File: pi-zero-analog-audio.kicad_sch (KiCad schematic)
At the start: 6 parts, among them J1 GPIO, U1 CAT24C256

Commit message: Unrouted
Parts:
- removed C1: 100n, symbol Device:C_Small
- removed JP1: ID_WP, symbol Jumper:SolderJumper_2_Open
- removed R1, R2: 3.9k, symbol Device:R_Small
- removed U1: CAT24C256, symbol Memory_EEPROM:CAT24C256
- added C1: 1u, Capacitor_SMD:C_0805_2012Metric_Pad1.18x1.45mm_HandSolder, symbol Device:C
- added C2: 4.7u, Capacitor_SMD:C_0805_2012Metric_Pad1.18x1.45mm_HandSolder, symbol Device:C
- added C3, C6: 47u, Capacitor_SMD:C_0805_2012Metric_Pad1.18x1.45mm_HandSolder, symbol Device:C_Polarized
- added C4, C5, C7: 100n, Capacitor_SMD:C_0805_2012Metric_Pad1.18x1.45mm_HandSolder, symbol Device:C
- added J2: SJ1-3555NG-BE, CUI_SJ1-3555NG-BE, symbol SJ1-3555NG-BE:SJ1-3555NG-BE
- added R1, R4: 220R, Resistor_SMD:R_0805_2012Metric_Pad1.20x1.40mm_HandSolder, symbol Device:R
- added R2, R5: 100R, Resistor_SMD:R_0805_2012Metric_Pad1.20x1.40mm_HandSolder, symbol Device:R
- added R3, R6: 1.8k, Resistor_SMD:R_0805_2012Metric_Pad1.20x1.40mm_HandSolder, symbol Device:R
- added U1: LP5907MFX-3.3, Package_TO_SOT_SMD:SOT-23-5, symbol Regulator_Linear:LP5907MFX-3.3
- added U2: 74LVC2G34, Package_TO_SOT_SMD:SOT-23-6_Handsoldering, symbol 74xGxx:74LVC2G34
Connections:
- net +5V: now also C1.1, U1.1 (IN), U1.3 (EN)
- net GND: now also C1.2, C2.2, C4.2, C5.2, C7.2, J2.1, R2.2, R3.2, R5.2, R6.2, U1.2 (GND), U2.2 (GND), U2.2 (GND)
- net +3V3 renamed +3.3V
- net GPIO26: no longer names the net of J1.37 (Pin_37)
- net GPIO[10]/SPI0.MOSI: no longer names the net of J1.19 (Pin_19)
- net GPIO[11]/SPI0.SCLK: no longer names the net of J1.23 (Pin_23)
- net GPIO[12]/PWM0 renamed PWM0
- net PWM0: now also U2.3
- net GPIO[13]/PWM1 renamed PWM1
- net PWM1: now also U2.1
- net GPIO[14]/TXD0: no longer names the net of J1.8 (Pin_8)
- net GPIO[15]/RXD0: no longer names the net of J1.10 (Pin_10)
- net GPIO[16]: no longer names the net of J1.36 (Pin_36)
- net GPIO[17]: no longer names the net of J1.11 (Pin_11)
- net GPIO[18]/PCM.CLK: no longer names the net of J1.12 (Pin_12)
- net GPIO[19]/PCM.FS: no longer names the net of J1.35 (Pin_35)
- net GPIO[20]/PCM.DIN: no longer names the net of J1.38 (Pin_38)
- net GPIO[21]/PCM.DOUT: no longer names the net of J1.40 (Pin_40)
- net GPIO[22]: no longer names the net of J1.15 (Pin_15)
- net GPIO[23]: no longer names the net of J1.16 (Pin_16)
- net GPIO[24]: no longer names the net of J1.18 (Pin_18)
- net GPIO[25]: no longer names the net of J1.22 (Pin_22)
- net GPIO[27]: no longer names the net of J1.13 (Pin_13)
- net GPIO[2]/SDA1: no longer names the net of J1.3 (Pin_3)
- net GPIO[3]/SCL1: no longer names the net of J1.5 (Pin_5)
- net GPIO[4]/GPCLK0: no longer names the net of J1.7 (Pin_7)
- net GPIO[5]: no longer names the net of J1.29 (Pin_29)
- net GPIO[6]: no longer names the net of J1.31 (Pin_31)
- net GPIO[7]/SPI0.CE1: no longer names the net of J1.26 (Pin_26)
- net GPIO[8]/SPI0.CE0: no longer names the net of J1.24 (Pin_24)
- net GPIO[9]/SPI0.MISO: no longer names the net of J1.21 (Pin_21)
- net ID_SCL: no longer names the net of J1.28 (Pin_28)
- net ID_SDA: no longer names the net of J1.27 (Pin_27)
- new net: R1.2, U2.6
- new net: C6.1, C7.1, R4.1, R5.1
- new net: R4.2, U2.4
- new net: C3.1, C4.1, R1.1, R2.1
- new net AUDIO_L: C3.2, J2.2, R3.1
- new net AUDIO_R: C6.2, J2.3, R6.1
- new net VCC: C2.1, C5.1, U1.5 (OUT), U2.5 (VCC), U2.5 (VCC)
- no-connect marks 3 -> 26
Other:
- note removed: "ID_SD and ID_SC PINS: These pins are reserved for HAT ID EEPROM. At boot time this I2C interface will be interrogated to look for an EEPROM that identifes the attached board and allows automagic setup of the GPIOs (and optionally, Linux drivers). Bridging JP1 enables write protection. DO NOT USE these pins for anything other than attaching an I2C ID EEPROM. Leave unconnected if ID EEPROM not requ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"
- moved on the sheet: J1

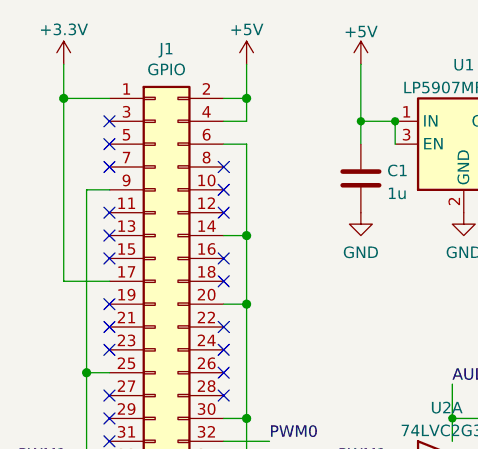
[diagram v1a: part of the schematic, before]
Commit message: we are using internal symbol libraries
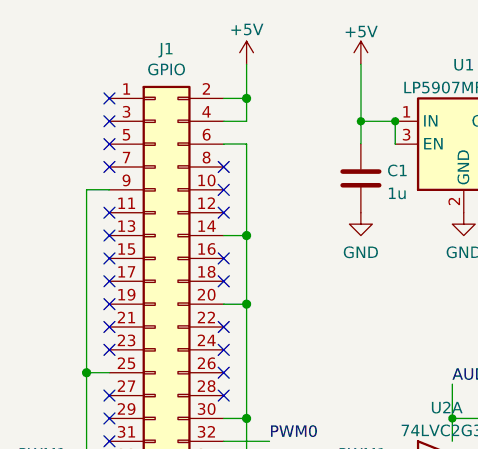
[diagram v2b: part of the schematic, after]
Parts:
- J2: footprint CUI_SJ1-3555NG-BE -> library:CUI_SJ1-3555NG-BE
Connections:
- net +3.3V: no longer names the net of J1.1 (Pin_1)
- net +3.3V: no longer J1.17 (Pin_17)
- no-connect marks 26 -> 28
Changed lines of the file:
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@@
   (junction (at 40.64 59.69) (diameter 1.016) (color 0 0 0 0)
-  )
-  (junction (at 20.32 24.13) (diameter 1.016) (color 0 0 0 0)
   )
   (junction (at 40.64 64.77) (diameter 1.016) (color 0 0 0 0)
@@
   (no_connect (at 38.1 72.39))
   (no_connect (at 38.1 52.07))
+  (no_connect (at 25.4 24.13))
+  (no_connect (at 25.4 44.45))
   (no_connect (at 25.4 69.85))
   (no_connect (at 25.4 49.53))
@@
     (stroke (width 0) (type default) (color 0 0 0 0))
   )
-  (wire (pts (xy 20.32 20.32) (xy 20.32 24.13))
-    (stroke (width 0) (type solid) (color 0 0 0 0))
-  )
   (wire (pts (xy 63.5 78.74) (xy 63.5 86.36))
     (stroke (width 0) (type default) (color 0 0 0 0))
@@
     (stroke (width 0) (type default) (color 0 0 0 0))
   )
-  (wire (pts (xy 20.32 44.45) (xy 25.4 44.45))
-    (stroke (width 0) (type solid) (color 0 0 0 0))
-  )
   (wire (pts (xy 40.64 24.13) (xy 40.64 26.67))
     (stroke (width 0) (type solid) (color 0 0 0 0))
@@
     (stroke (width 0) (type solid) (color 0 0 0 0))
   )
-  (wire (pts (xy 20.32 24.13) (xy 20.32 44.45))
-    (stroke (width 0) (type solid) (color 0 0 0 0))
-  )
   (wire (pts (xy 72.39 26.67) (xy 74.93 26.67))
     (stroke (width 0) (type default) (color 0 0 0 0))
@@
   )
   (wire (pts (xy 40.64 59.69) (xy 38.1 59.69))
-    (stroke (width 0) (type solid) (color 0 0 0 0))
-  )
-  (wire (pts (xy 20.32 24.13) (xy 25.4 24.13))
     (stroke (width 0) (type solid) (color 0 0 0 0))
   )
@@
     (property "Footprint" "" (id 2) (at 40.64 20.32 0))
     (property "Datasheet" "" (id 3) (at 40.64 20.32 0))
-    (pin "1")
-  )
-  (symbol (lib_id "power:+3.3V") (at 20.32 20.32 0) (unit 1)
-    (in_bom yes) (on_board yes)
-    (property "Reference" "#PWR01" (id 0) (at 20.32 24.13 0)
-      (effects (font (size 1.27 1.27)) hide)
-    )
-    (property "Value" "+3.3V" (id 1) (at 20.32 16.51 0))
-    (property "Footprint" "" (id 2) (at 20.32 20.32 0))
-    (property "Datasheet" "" (id 3) (at 20.32 20.32 0))
     (pin "1")
   )
@@
       (effects (font (size 1.27 1.27)) (justify right))
     )
-    (property "Footprint" "CUI_SJ1-3555NG-BE" (id 2) (at 154.94 73.66 0)
+    (property "Footprint" "library:CUI_SJ1-3555NG-BE" (id 2) (at 154.94 73.66 0)
       (effects (font (size 1.27 1.27)) (justify left bottom) hide)
     )
@@
   )
   (symbol_instances
-    (path "/00000000-0000-0000-0000-0000580c1bc1"
-      (reference "#PWR01") (unit 1) (value "+3.3V") (footprint "")
-    )
     (path "/00000000-0000-0000-0000-0000580c1b61"
       (reference "#PWR02") (unit 1) (value "+5V") (footprint "")
@@
     )
     (path "/0b4362dd-e0ca-493b-8fc1-107bd0984034"
-      (reference "J2") (unit 1) (value "SJ1-3555NG-BE") (footprint "CUI_SJ1-3555NG-BE")
+      (reference "J2") (unit 1) (value "SJ1-3555NG-BE") (footprint "library:CUI_SJ1-3555NG-BE")
     )
     (path "/72d935ce-432c-4183-b481-300609728f6c"

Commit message: Another day starts
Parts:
- added C8: 470u, Capacitor_THT:CP_Radial_D8.0mm_P3.50mm, symbol Device:C_Polarized
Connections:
- net +5V: now also C8.1
- net GND: now also C8.2
- net AMP_L: now reaches J2.4
- net AMP_R: now reaches J2.5
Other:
- moved on the sheet: C1, C2, C3, C4, C5, C6, C7, J2, R1, R2, R3, R4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

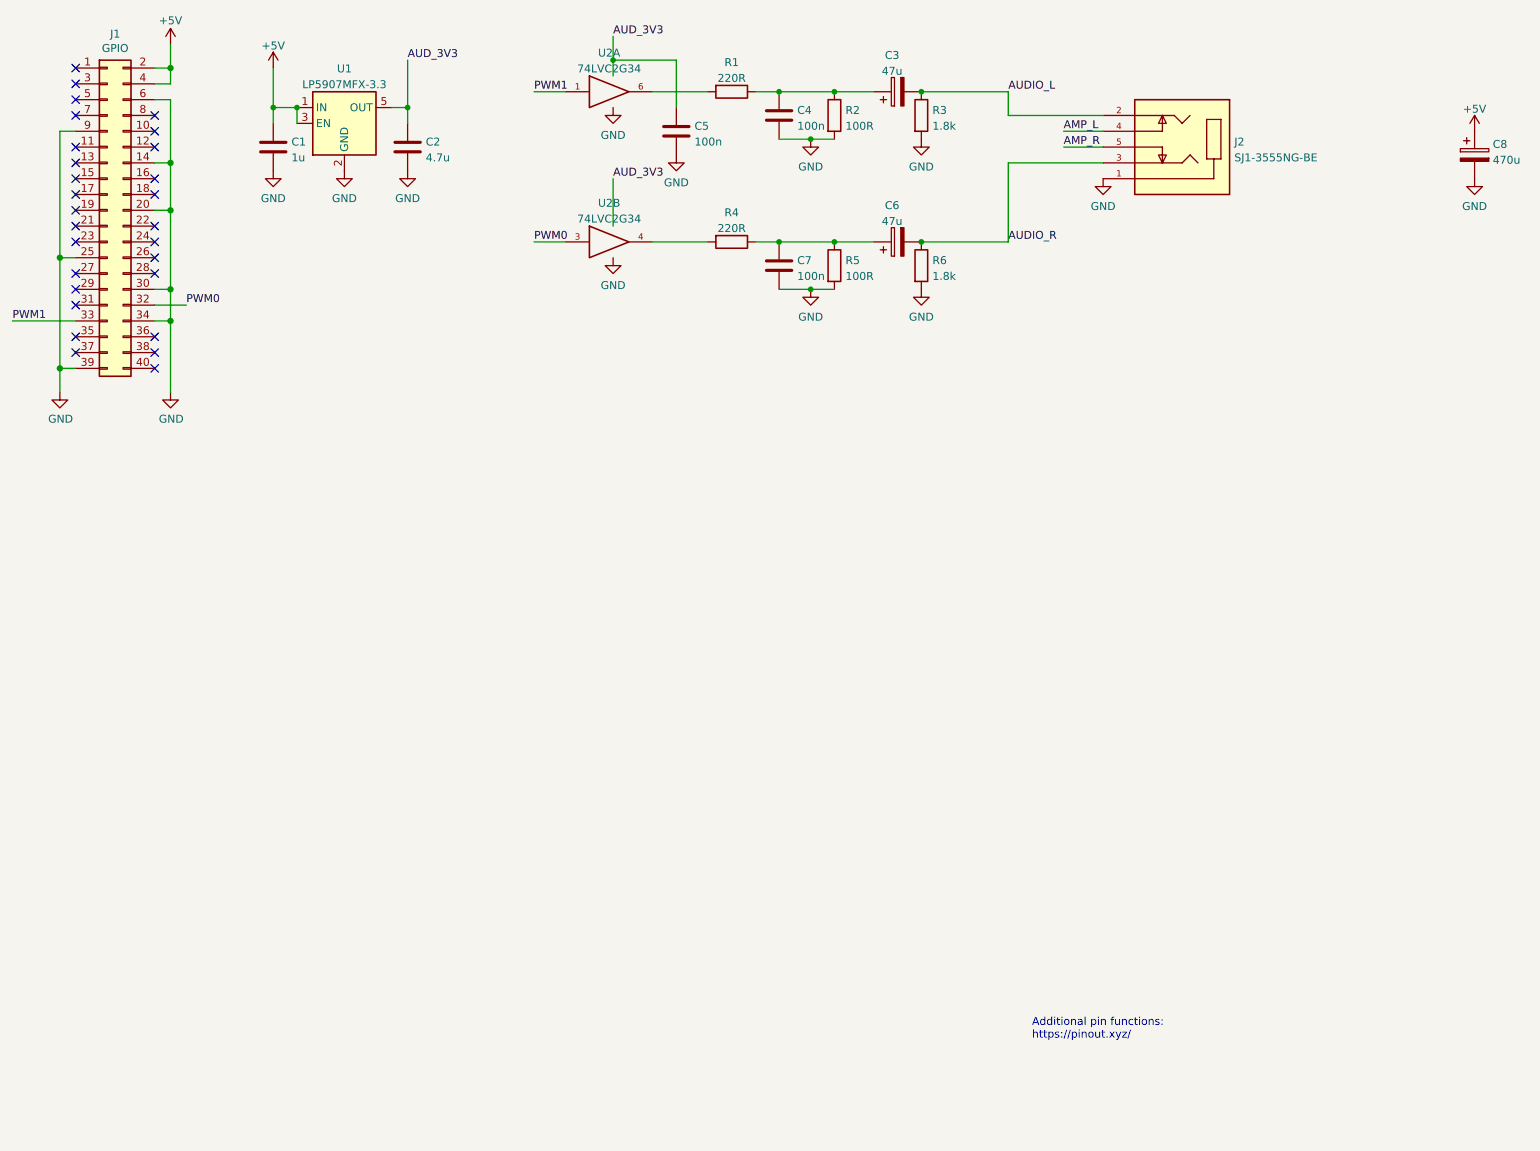
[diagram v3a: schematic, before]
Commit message: Adding a connector for a possible Class-D amplifier
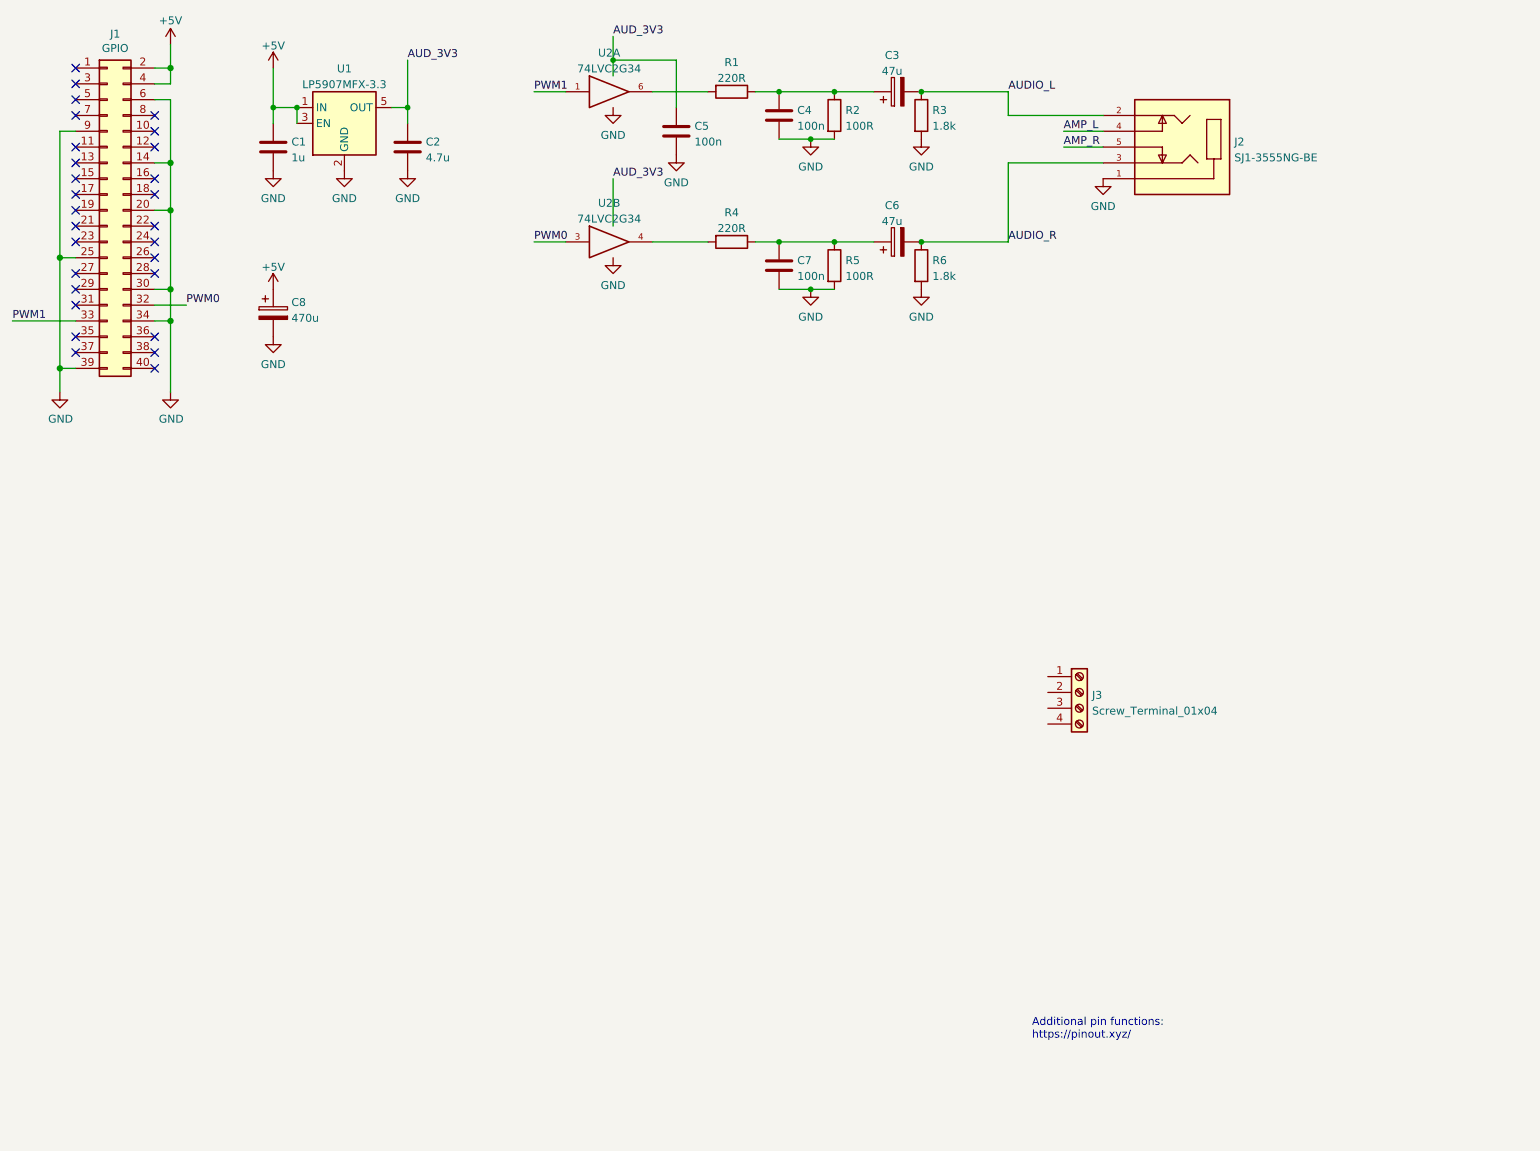
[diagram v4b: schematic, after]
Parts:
- added J3: Screw_Terminal_01x04, TerminalBlock:TerminalBlock_bornier-4_P5.08mm, symbol Connector:Screw_Terminal_01x04
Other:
- moved on the sheet: C8
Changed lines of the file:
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@@
     (pin "9")
   )
-  (symbol (lib_id "Device:C_Polarized") (at 250.19 38.1 0) (unit 1)
-    (in_bom yes) (on_board yes) (fields_autoplaced)
-    (property "Reference" "C8" (id 0) (at 253.111 36.3763 0)
-      (effects (font (size 1.27 1.27)) (justify left))
-    )
-    (property "Value" "470u" (id 1) (at 253.111 38.9132 0)
-      (effects (font (size 1.27 1.27)) (justify left))
-    )
-    (property "Footprint" "Capacitor_THT:CP_Radial_D8.0mm_P3.50mm" (id 2) (at 251.1552 41.91 0)
-      (effects (font (size 1.27 1.27)) hide)
-    )
-    (property "Datasheet" "~" (id 3) (at 250.19 38.1 0)
+  (symbol (lib_id "Device:C_Polarized") (at 57.15 63.5 0) (unit 1)
+    (in_bom yes) (on_board yes) (fields_autoplaced)
+    (property "Reference" "C8" (id 0) (at 60.071 61.7763 0)
+      (effects (font (size 1.27 1.27)) (justify left))
+    )
+    (property "Value" "470u" (id 1) (at 60.071 64.3132 0)
+      (effects (font (size 1.27 1.27)) (justify left))
+    )
+    (property "Footprint" "Capacitor_THT:CP_Radial_D8.0mm_P3.50mm" (id 2) (at 58.1152 67.31 0)
+      (effects (font (size 1.27 1.27)) hide)
+    )
+    (property "Datasheet" "~" (id 3) (at 57.15 63.5 0)
       (effects (font (size 1.27 1.27)) hide)
     )
@@
     (pin "2")
   )
-  (symbol (lib_id "power:GND") (at 250.19 41.91 0) (unit 1)
-    (in_bom yes) (on_board yes) (fields_autoplaced)
-    (property "Reference" "#PWR017" (id 0) (at 250.19 48.26 0)
-      (effects (font (size 1.27 1.27)) hide)
-    )
-    (property "Value" "GND" (id 1) (at 250.19 46.3534 0))
-    (property "Footprint" "" (id 2) (at 250.19 41.91 0)
-      (effects (font (size 1.27 1.27)) hide)
-    )
-    (property "Datasheet" "" (id 3) (at 250.19 41.91 0)
+  (symbol (lib_id "power:GND") (at 57.15 67.31 0) (unit 1)
+    (in_bom yes) (on_board yes) (fields_autoplaced)
+    (property "Reference" "#PWR017" (id 0) (at 57.15 73.66 0)
+      (effects (font (size 1.27 1.27)) hide)
+    )
+    (property "Value" "GND" (id 1) (at 57.15 71.7534 0))
+    (property "Footprint" "" (id 2) (at 57.15 67.31 0)
+      (effects (font (size 1.27 1.27)) hide)
+    )
+    (property "Datasheet" "" (id 3) (at 57.15 67.31 0)
       (effects (font (size 1.27 1.27)) hide)
     )
@@
     (pin "1")
   )
-  (symbol (lib_id "power:+5V") (at 250.19 34.29 0) (unit 1)
+  (symbol (lib_id "power:+5V") (at 57.15 59.69 0) (unit 1)
     (in_bom yes) (on_board yes)
-    (property "Reference" "#PWR01" (id 0) (at 250.19 38.1 0)
-      (effects (font (size 1.27 1.27)) hide)
-    )
-    (property "Value" "+5V" (id 1) (at 250.19 30.7142 0))
-    (property "Footprint" "" (id 2) (at 250.19 34.29 0)
-      (effects (font (size 1.27 1.27)) hide)
-    )
-    (property "Datasheet" "" (id 3) (at 250.19 34.29 0)
+    (property "Reference" "#PWR01" (id 0) (at 57.15 63.5 0)
+      (effects (font (size 1.27 1.27)) hide)
+    )
+    (property "Value" "+5V" (id 1) (at 57.15 56.1142 0))
+    (property "Footprint" "" (id 2) (at 57.15 59.69 0)
+      (effects (font (size 1.27 1.27)) hide)
+    )
+    (property "Datasheet" "" (id 3) (at 57.15 59.69 0)
       (effects (font (size 1.27 1.27)) hide)
     )
@@
     (pin "1")
   )
+  (symbol (lib_id "Connector:Screw_Terminal_01x04") (at 186.69 124.46 0) (unit 1)
+    (in_bom yes) (on_board yes) (fields_autoplaced)
+    (property "Reference" "J3" (id 0) (at 188.722 124.8953 0)
+      (effects (font (size 1.27 1.27)) (justify left))
+    )
+    (property "Value" "Screw_Terminal_01x04" (id 1) (at 188.722 127.4322 0)
+      (effects (font (size 1.27 1.27)) (justify left))
+    )
+    (property "Footprint" "TerminalBlock:TerminalBlock_bornier-4_P5.08mm" (id 2) (at 186.69 124.46 0)
+      (effects (font (size 1.27 1.27)) hide)
+    )
+    (property "Datasheet" "~" (id 3) (at 186.69 124.46 0)
+      (effects (font (size 1.27 1.27)) hide)
+    )
+    (pin "1")
+    (pin "2")
+    (pin "3")
+    (pin "4")
+  )
   (symbol (lib_id "power:GND") (at 111.76 54.61 0) (unit 1)
     (in_bom yes) (on_board yes) (fields_autoplaced)
@@
       (reference "J2") (unit 1) (value "SJ1-3555NG-BE") (footprint "library:CUI_SJ1-3555NG-BE")
     )
+    (path "/e4e0ca7e-6acb-48b6-bf2b-4d2939783b7f"
+      (reference "J3") (unit 1) (value "Screw_Terminal_01x04") (footprint "TerminalBlock:TerminalBlock_bornier-4_P5.08mm")
+    )
     (path "/72d935ce-432c-4183-b481-300609728f6c"
